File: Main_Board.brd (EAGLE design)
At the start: 160 x 100 mm, 54 parts, among them U1 RN4020RN4020, Y1 MC-30632.768K-E3, Y2 MA-5066-25.0000M-C0

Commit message: added buck regulator
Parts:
- removed S1: (no value), SparkFun-Electromechanical:SWITCH-SPDT_LOCK.007S
- removed U$11: SWITCH-SPST-2RA, SparkFun-Electromechanical:R_SW_TH
- removed U$8: LMS8117, BB8:SOT-223
- added JP1: SPDT_JUMPER, BB8:1X03
- added S2: RESET_BUTTON, BB8:5.2X5.2
- added U2: LMS8117, BB8:SOT-223
- moved FRAME4 125.5 mm to (-195.0, -178.0)
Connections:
- net 3.3V: now also JP1.3, U2.P$2, U2.P$4; no longer S1.3, U$8.P$2, U$8.P$4
- net 5V: now also U2.P$3; no longer U$8.P$3
- net GND: now also JP1.1, S2.P$3, S2.P$4, U2.P$1; no longer S1.1, U$11.P$4, U$8.P$1
- net N$23: now also JP1.2; no longer S1.2
- net N$7: now also S2.P$1, S2.P$2; no longer U$11.P$3
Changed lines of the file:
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@@
 <element name="C12" library="SparkFun-Capacitors" package="0805" value="2.2uF" x="-107" y="-95"/>
 <element name="FRAME2" library="SparkFun-Aesthetics" package="CREATIVE_COMMONS" value="FRAME-LEDGER" x="-87" y="-105"/>
-<element name="FRAME4" library="SparkFun-Aesthetics" package="CREATIVE_COMMONS" value="FRAME-LEDGER" x="-87" y="-114"/>
 <element name="FRAME1" library="SparkFun-Aesthetics" package="CREATIVE_COMMONS" value="FRAME-LEDGER" x="-87" y="-123"/>
 <element name="FRAME3" library="SparkFun-Aesthetics" package="CREATIVE_COMMONS" value="FRAME-LEDGER" x="-87" y="-132"/>
-<element name="U$8" library="BB8" package="SOT-223" value="LMS8117" x="-113" y="-132"/>
 <element name="C13" library="SparkFun-Capacitors" package="0805" value="" x="-118" y="-131"/>
 <element name="C14" library="SparkFun-Capacitors" package="0805" value="" x="-121" y="-131"/>
@@
 <element name="U$10" library="BB8" package="14-TSSOP" value="SN74LV4T125" x="-133" y="-132"/>
 <element name="C15" library="SparkFun-Capacitors" package="0805" value="4.7uF" x="-136" y="-131"/>
-<element name="U$11" library="SparkFun-Electromechanical" package="R_SW_TH" value="SWITCH-SPST-2RA" x="-152" y="-130"/>
 <element name="C16" library="SparkFun-Passives" package="0805" value=".1uF" x="-156" y="-131"/>
 <element name="C17" library="SparkFun-Passives" package="0805" value="6.8pF" x="-159" y="-137"/>
@@
 <element name="R11" library="SparkFun-Passives" package="0805" value="220" x="-171" y="-143"/>
 <element name="R12" library="SparkFun-Passives" package="0805" value="0" x="-174" y="-143"/>
-<element name="S1" library="SparkFun-Electromechanical" package="SWITCH-SPDT_LOCK.007S" value="" x="-182" y="-134"/>
 <element name="R13" library="SparkFun-Passives" package="0805" value="10K" x="-188" y="-143"/>
 <element name="R14" library="SparkFun-Passives" package="0805" value="0" x="-191" y="-143"/>
@@
 <element name="Y1" library="BB8" package="4-SMD,J-LEAD" value="MC-30632.768K-E3" x="-193" y="-150"/>
 <element name="Y2" library="BB8" package="4-SMD,J-LEAD-2" value="MA-5066-25.0000M-C0" x="-193" y="-158"/>
+<element name="S2" library="BB8" package="5.2X5.2" value="RESET_BUTTON" x="-194" y="-167"/>
+<element name="JP1" library="BB8" package="1X03" value="SPDT_JUMPER" x="-192" y="-174"/>
+<element name="FRAME4" library="SparkFun-Aesthetics" package="CREATIVE_COMMONS" value="FRAME-LEDGER" x="-195" y="-178"/>
+<element name="U2" library="BB8" package="SOT-223" value="LMS8117" x="-200" y="-178"/>
 </elements>
 <signals>
@@
 <contactref element="C11" pad="2"/>
 <contactref element="C13" pad="2"/>
-<contactref element="U$8" pad="P$1"/>
 <contactref element="C14" pad="2"/>
 <contactref element="U$9" pad="P$1"/>
@@
 <contactref element="U$10" pad="P$9"/>
 <contactref element="C15" pad="1"/>
-<contactref element="U$11" pad="P$4"/>
 <contactref element="C16" pad="1"/>
-<contactref element="S1" pad="1"/>
 <contactref element="C17" pad="1"/>
 <contactref element="C18" pad="1"/>
@@
 <contactref element="C19" pad="1"/>
 <contactref element="C16" pad="2"/>
+<contactref element="S2" pad="P$3"/>
+<contactref element="S2" pad="P$4"/>
+<contactref element="JP1" pad="1"/>
+<contactref element="U2" pad="P$1"/>
 <wire x1="-125.05" y1="-132" x2="-123.1" y2="-132" width="0" layer="19" extent="1-1"/>
 <wire x1="-127" y1="-132" x2="-125.05" y2="-132" width="0" layer="19" extent="1-1"/>
@@
 <wire x1="-120.1" y1="-131" x2="-123.1" y2="-132" width="0" layer="19" extent="1-1"/>
 <wire x1="-117.1" y1="-131" x2="-120.1" y2="-131" width="0" layer="19" extent="1-1"/>
-<wire x1="-115.3" y1="-132" x2="-117.1" y2="-131" width="0" layer="19" extent="1-1"/>
 <wire x1="-136.9" y1="-131" x2="-133" y2="-132" width="0" layer="19" extent="1-1"/>
 <wire x1="-126.35" y1="-126.4" x2="-127" y2="-132" width="0" layer="19" extent="1-1"/>
@@
 <wire x1="-129.75" y1="-126.4" x2="-126.35" y2="-126.4" width="0" layer="19" extent="1-1"/>
 <wire x1="-131.7" y1="-126.4" x2="-129.75" y2="-126.4" width="0" layer="19" extent="1-1"/>
-<wire x1="-139.9096" y1="-121.5418" x2="-131.7" y2="-126.4" width="0" layer="19" extent="1-1"/>
-<wire x1="-155.1" y1="-131" x2="-139.9096" y2="-121.5418" width="0" layer="19" extent="1-1"/>
+<wire x1="-155.1" y1="-131" x2="-136.9" y2="-131" width="0" layer="19" extent="1-1"/>
 <wire x1="-156.9" y1="-131" x2="-155.1" y2="-131" width="0" layer="19" extent="1-1"/>
 <wire x1="-159.9" y1="-137" x2="-156.9" y2="-131" width="0" layer="19" extent="1-1"/>
@@
 <wire x1="-165.9" y1="-143" x2="-162.9" y2="-137" width="0" layer="19" extent="1-1"/>
 <wire x1="-168.9" y1="-143" x2="-165.9" y2="-143" width="0" layer="19" extent="1-1"/>
-<wire x1="-182" y1="-131.2822" x2="-168.9" y2="-143" width="0" layer="19" extent="1-1"/>
+<wire x1="-188.1" y1="-163.3" x2="-168.9" y2="-143" width="0" layer="19" extent="1-1"/>
+<wire x1="-194" y1="-163.3" x2="-188.1" y2="-163.3" width="0" layer="19" extent="1-1"/>
+<wire x1="-192" y1="-174" x2="-194" y2="-163.3" width="0" layer="19" extent="1-1"/>
+<wire x1="-202.3" y1="-178" x2="-192" y2="-174" width="0" layer="19" extent="1-1"/>
 <wire x1="-106.1" y1="-95" x2="-124.4" y2="-126.4" width="0" layer="19" extent="1-1"/>
 <wire x1="-103.1" y1="-95" x2="-106.1" y2="-95" width="0" layer="19" extent="1-1"/>
@@
 <contactref element="U$3" pad="VCC"/>
 <contactref element="U$4" pad="VCC"/>
-<contactref element="U$8" pad="P$3"/>
 <contactref element="C13" pad="1"/>
 <contactref element="U$10" pad="P$14"/>
 <contactref element="U$10" pad="P$13"/>
 <contactref element="U$10" pad="P$10"/>
-<wire x1="-110.7" y1="-132" x2="-118.9" y2="-131" width="0" layer="19" extent="1-1"/>
+<contactref element="U2" pad="P$3"/>
 <wire x1="-130.4" y1="-126.4" x2="-118.9" y2="-131" width="0" layer="19" extent="1-1"/>
 <wire x1="-132.35" y1="-126.4" x2="-130.4" y2="-126.4" width="0" layer="19" extent="1-1"/>
 <wire x1="-133" y1="-126.4" x2="-132.35" y2="-126.4" width="0" layer="19" extent="1-1"/>
-<wire x1="-40.64" y1="-35.56" x2="-110.7" y2="-132" width="0" layer="19" extent="1-1"/>
+<wire x1="-197.7" y1="-178" x2="-133" y2="-126.4" width="0" layer="19" extent="1-1"/>
+<wire x1="-40.64" y1="-35.56" x2="-118.9" y2="-131" width="0" layer="19" extent="1-1"/>
 <wire x1="-15.24" y1="-13.97" x2="-40.64" y2="-35.56" width="0" layer="19" extent="1-1"/>
 </signal>
@@
 <contactref element="C10" pad="2"/>
 <contactref element="C9" pad="2"/>
-<contactref element="U$8" pad="P$2"/>
-<contactref element="U$8" pad="P$4"/>
 <contactref element="C14" pad="1"/>
 <contactref element="U$9" pad="P$14"/>
 <contactref element="U1" pad="P$23"/>
 <contactref element="C15" pad="2"/>
-<contactref element="S1" pad="3"/>
+<contactref element="JP1" pad="3"/>
+<contactref element="U2" pad="P$4"/>
+<contactref element="U2" pad="P$2"/>
 <wire x1="-121.9" y1="-131" x2="-127" y2="-126.4" width="0" layer="19" extent="1-1"/>
-<wire x1="-113" y1="-132" x2="-121.9" y2="-131" width="0" layer="19" extent="1-1"/>
-<wire x1="-113" y1="-125.7" x2="-113" y2="-132" width="0" layer="19" extent="1-1"/>
 <wire x1="-135.1" y1="-131" x2="-127" y2="-126.4" width="0" layer="19" extent="1-1"/>
-<wire x1="-100.1" y1="-95" x2="-113" y2="-125.7" width="0" layer="19" extent="1-1"/>
+<wire x1="-100.1" y1="-95" x2="-127" y2="-126.4" width="0" layer="19" extent="1-1"/>
 <wire x1="-97.1" y1="-95" x2="-100.1" y2="-95" width="0" layer="19" extent="1-1"/>
 <wire x1="-95.9" y1="-95" x2="-97.1" y2="-95" width="0" layer="19" extent="1-1"/>
@@
 <wire x1="-38.05" y1="-69.55" x2="-38.05" y2="-76.05" width="0" layer="19" extent="1-1"/>
 <wire x1="-47.55" y1="-67.55" x2="-49.55" y2="-77.05" width="0" layer="19" extent="1-1"/>
-<wire x1="-182" y1="-136.7178" x2="-135.1" y2="-131" width="0" layer="19" extent="1-1"/>
+<wire x1="-186.92" y1="-174" x2="-135.1" y2="-131" width="0" layer="19" extent="1-1"/>
+<wire x1="-200" y1="-171.7" x2="-186.92" y2="-174" width="0" layer="19" extent="1-1"/>
+<wire x1="-200" y1="-178" x2="-200" y2="-171.7" width="0" layer="19" extent="1-1"/>
 </signal>
 <signal name="N$15">
@@
 <signal name="N$7">
 <contactref element="U$5" pad="P$7"/>
-<contactref element="U$11" pad="P$3"/>
-<wire x1="-139.9096" y1="-114.506" x2="-44.55" y2="-79.05" width="0" layer="19" extent="1-1"/>
+<contactref element="S2" pad="P$1"/>
+<contactref element="S2" pad="P$2"/>
+<wire x1="-188.1" y1="-167" x2="-44.55" y2="-79.05" width="0" layer="19" extent="1-1"/>
+<wire x1="-194" y1="-167" x2="-188.1" y2="-167" width="0" layer="19" extent="1-1"/>
 </signal>
 <signal name="N$17">
@@
 <signal name="N$23">
 <contactref element="R13" pad="1"/>
-<contactref element="S1" pad="2"/>
-<wire x1="-182" y1="-134" x2="-188.9" y2="-143" width="0" layer="19" extent="1-1"/>
+<contactref element="JP1" pad="2"/>
+<wire x1="-188.9" y1="-143" x2="-189.46" y2="-174" width="0" layer="19" extent="1-1"/>
 </signal>
 <signal name="N$24">

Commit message: added jtag
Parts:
- added L1: (no value), SparkFun-Passives:0805
- added U$11: 1000uF, BB8:RADIAL_CAN_SMD
- added U$12: JTAG, BB8:IDC20
- added U$8: 100uF, BB8:RADIAL_CAN_SMD
- added U3: 5V_BUCK_REG, BB8:T0-263-6
- added Z1: SCHOTTKY_DIODE, BB8:DO-214AB2
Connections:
- new net N$31: L1.2, U3.P$2, Z1.C
- new net N$32: L1.1, U$11.P$1, U3.P$4
- net GND: now also U$11.P$2, U$8.P$2, U3.P$3, U3.P$5, U3.P$6, Z1.A
- net VCC: now also U$8.P$1, U3.P$1
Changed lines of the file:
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@@
 <element name="FRAME4" library="SparkFun-Aesthetics" package="CREATIVE_COMMONS" value="FRAME-LEDGER" x="-195" y="-178"/>
 <element name="U2" library="BB8" package="SOT-223" value="LMS8117" x="-200" y="-178"/>
+<element name="U3" library="BB8" package="T0-263-6" value="5V_BUCK_REG" x="-189" y="-189"/>
+<element name="U$8" library="BB8" package="RADIAL_CAN_SMD" value="100uF" x="-210" y="-190"/>
+<element name="Z1" library="BB8" package="DO-214AB2" value="SCHOTTKY_DIODE" x="-211" y="-195"/>
+<element name="L1" library="SparkFun-Passives" package="0805" value="" x="-215" y="-197"/>
+<element name="U$11" library="BB8" package="RADIAL_CAN_SMD" value="1000uF" x="-220" y="-198"/>
+<element name="U$12" library="BB8" package="IDC20" value="JTAG" x="-220" y="-205"/>
 </elements>
 <signals>
@@
 <contactref element="JP1" pad="1"/>
 <contactref element="U2" pad="P$1"/>
+<contactref element="U3" pad="P$5"/>
+<contactref element="U3" pad="P$3"/>
+<contactref element="U3" pad="P$6"/>
+<contactref element="U$8" pad="P$2"/>
+<contactref element="Z1" pad="A"/>
+<contactref element="U$11" pad="P$2"/>
 <wire x1="-125.05" y1="-132" x2="-123.1" y2="-132" width="0" layer="19" extent="1-1"/>
 <wire x1="-127" y1="-132" x2="-125.05" y2="-132" width="0" layer="19" extent="1-1"/>
@@
 <wire x1="-194" y1="-163.3" x2="-188.1" y2="-163.3" width="0" layer="19" extent="1-1"/>
 <wire x1="-192" y1="-174" x2="-194" y2="-163.3" width="0" layer="19" extent="1-1"/>
-<wire x1="-202.3" y1="-178" x2="-192" y2="-174" width="0" layer="19" extent="1-1"/>
+<wire x1="-189" y1="-182.2" x2="-192" y2="-174" width="0" layer="19" extent="1-1"/>
+<wire x1="-189" y1="-185.6" x2="-189" y2="-182.2" width="0" layer="19" extent="1-1"/>
+<wire x1="-199.675" y1="-185.6" x2="-189" y2="-185.6" width="0" layer="19" extent="1-1"/>
+<wire x1="-202.3" y1="-178" x2="-199.675" y2="-185.6" width="0" layer="19" extent="1-1"/>
+<wire x1="-210" y1="-185.6" x2="-199.675" y2="-185.6" width="0" layer="19" extent="1-1"/>
+<wire x1="-211" y1="-195" x2="-210" y2="-185.6" width="0" layer="19" extent="1-1"/>
+<wire x1="-220" y1="-193.6" x2="-211" y2="-195" width="0" layer="19" extent="1-1"/>
 <wire x1="-106.1" y1="-95" x2="-124.4" y2="-126.4" width="0" layer="19" extent="1-1"/>
 <wire x1="-103.1" y1="-95" x2="-106.1" y2="-95" width="0" layer="19" extent="1-1"/>
@@
 <contactref element="U$6" pad="P$1"/>
 <contactref element="U$7" pad="P$1"/>
+<contactref element="U3" pad="P$1"/>
+<contactref element="U$8" pad="P$1"/>
 <wire x1="-55" y1="-96" x2="-62" y2="-96" width="0" layer="19" extent="1-1"/>
 <wire x1="-50.43" y1="-40.64" x2="-55" y2="-96" width="0" layer="19" extent="1-1"/>
@@
 <wire x1="-1.7" y1="-1.09" x2="-1.7" y2="-1.74" width="0" layer="19" extent="1-1"/>
 <wire x1="-1.7" y1="-0.44" x2="-1.7" y2="-1.09" width="0" layer="19" extent="1-1"/>
+<wire x1="-189" y1="-189" x2="-62" y2="-96" width="0" layer="19" extent="1-1"/>
+<wire x1="-210" y1="-190" x2="-189" y2="-189" width="0" layer="19" extent="1-1"/>
 </signal>
 <signal name="N$1">
@@
 <wire x1="-158.1" y1="-137" x2="-191.9" y2="-143" width="0" layer="19" extent="1-1"/>
 </signal>
+<signal name="N$31">
+<contactref element="U3" pad="P$2"/>
+<contactref element="L1" pad="2"/>
+<contactref element="Z1" pad="C"/>
+<wire x1="-204.1" y1="-195" x2="-214.1" y2="-197" width="0" layer="19" extent="1-1"/>
+<wire x1="-189" y1="-187.3" x2="-204.1" y2="-195" width="0" layer="19" extent="1-1"/>
+</signal>
+<signal name="N$32">
+<contactref element="L1" pad="1"/>
+<contactref element="U$11" pad="P$1"/>
+<contactref element="U3" pad="P$4"/>
+<wire x1="-215.9" y1="-197" x2="-220" y2="-198" width="0" layer="19" extent="1-1"/>
+<wire x1="-189" y1="-183.9" x2="-215.9" y2="-197" width="0" layer="19" extent="1-1"/>
+</signal>
 </signals>

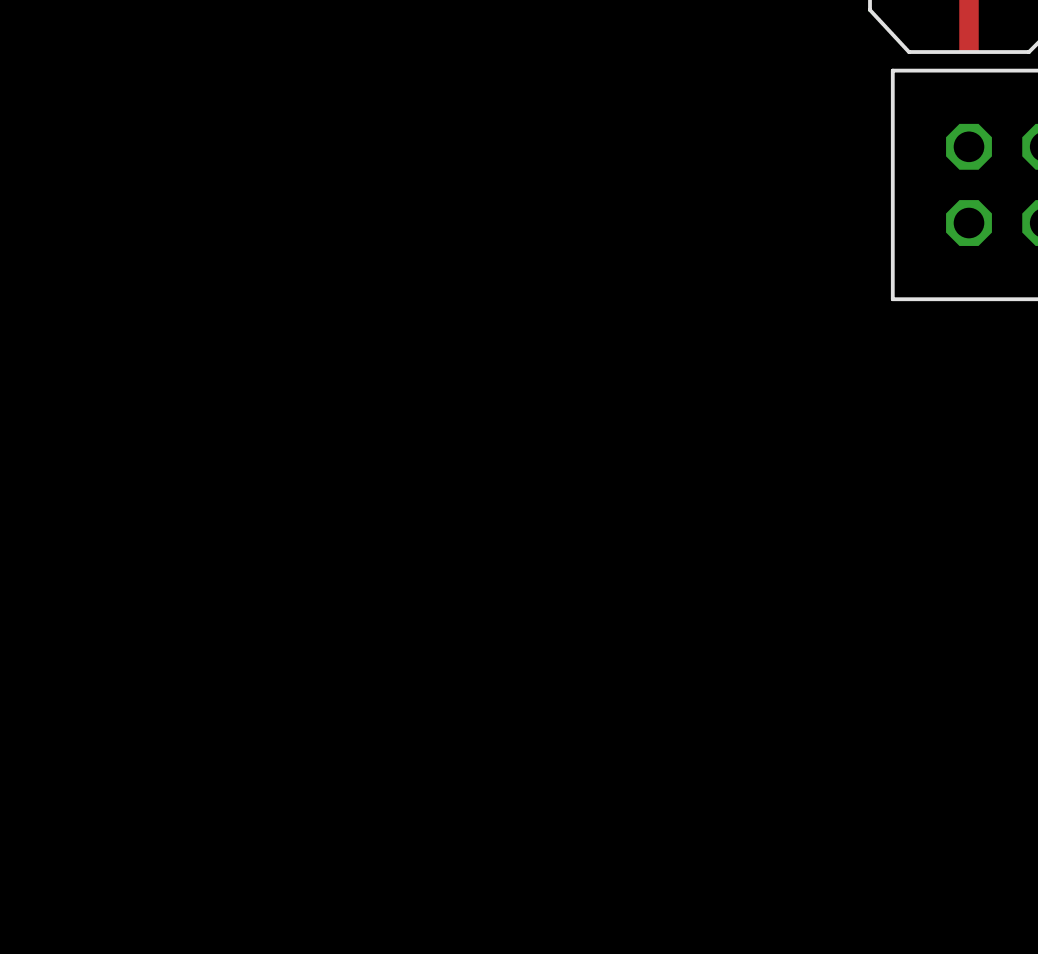
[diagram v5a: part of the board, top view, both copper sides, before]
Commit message: started adding motors
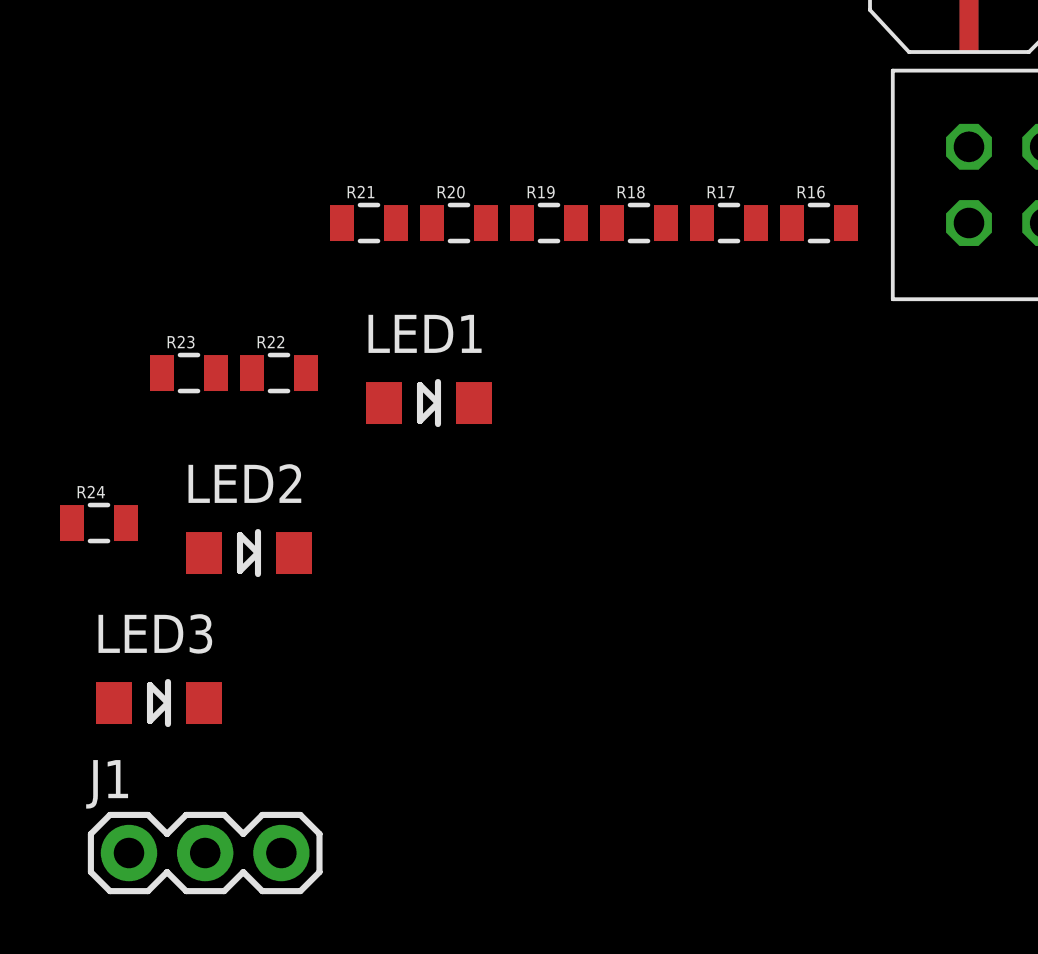
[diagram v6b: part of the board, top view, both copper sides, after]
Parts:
- added J1: (no value), SparkFun-Connectors:1X03
- added LED1, LED2, LED3: (no value), LilyPad-Wearables:LED-1206
- added R16, R17, R18, R19, R20, R21, R22, R23, R24: 10K, SparkFun-Passives:0805
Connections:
- new net !NRST: S2.P$1, S2.P$2, U$12.P$15, U$5.P$7
- new net BLUE_WAKE_SW: U$5.P$20, U1.P$7
- new net BLU_CTS: U$5.P$15, U1.P$14
- new net BLU_RTS: U$5.P$14, U1.P$18
- new net BLU_RX: U$5.P$16, U1.P$6
- new net BLU_TX: U$5.P$17, U1.P$5
- new net BLU_WAKE_HW: U$5.P$22, U1.P$15
- new net JNTRST: U$12.P$3, U$5.P$56
- new net JTCK: U$12.P$9, U$5.P$49
- new net JTDI: U$12.P$5, U$5.P$50
- new net JTDO: U$12.P$13, U$5.P$55
- new net JTMS: U$12.P$7, U$5.P$46
- new net N$33: U1.P$8
- new net N$34: R22.2, U1.P$10
- new net N$35: LED1.A, R22.1
- new net N$36: R23.2, U1.P$11
- new net N$37: R24.2, U1.P$12
- new net N$38: LED2.A, R23.1
- new net N$39: LED3.A, R24.1
- new net SERVO_PWM_3.3: U$10.P$9, U$5.P$41
- new net SERVO_PWM_5: U$10.P$8
- net 3.3V: now also U$12.P$1, U$12.P$2
- net 5V: no longer U$10.P$10
- net GND: now also LED1.C, LED2.C, LED3.C, R16.1, R17.1, R18.1, R19.1, R20.1, R21.1, U$10.P$10, U$12.P$10, U$12.P$12, U$12.P$14, U$12.P$16, U$12.P$18, U$12.P$20, U$12.P$4, U$12.P$6, U$12.P$8; no longer U$10.P$9
- net M1_A_3.3: now also U$5.P$23
- net M1_B_3.3: now also U$5.P$24
- net M2_A_3.3: now also U$5.P$25
- net M2_B_3.3: now also U$5.P$26
- net MC1_INH_3.3: now also U$5.P$40
- net MC2_IS: now also U$5.P$9
- net N$24: now also R16.2, U$12.P$11; no longer U$5.P$46
- net N$25: now also R17.2, U$12.P$17; no longer U$5.P$49
- net N$26: now also R18.2, U$12.P$19; no longer U$5.P$50
- net N$27: now also R20.2, U1.P$3; no longer U$5.P$55
- net N$28: now also R21.2, U1.P$4; no longer U$5.P$56
- net N$7: now also R19.2, U1.P$2; no longer S2.P$1, S2.P$2, U$5.P$7

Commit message: finished adding motors
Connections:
- removed net MC1_ING_3.3: U$10.P$5
- new net MC2_INH_3.3: U$5.P$39
- net MC1_IN1: now also U$5.P$38
- net MC1_IN2: now also U$5.P$37
- net MC1_INH_3.3: now also U$10.P$5
- net MC2_IN1: now also U$5.P$36
- net MC2_IN2: now also U$5.P$35
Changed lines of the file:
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@@
 <signal name="MC2_IN1">
 <contactref element="R6" pad="1"/>
+<contactref element="U$5" pad="P$36"/>
+<wire x1="-42.81" y1="-40.64" x2="-41.55" y2="-67.55" width="0" layer="19" extent="1-1"/>
 </signal>
 <signal name="MC2_IN2">
 <contactref element="R7" pad="1"/>
+<contactref element="U$5" pad="P$35"/>
+<wire x1="-39" y1="-40.64" x2="-41.05" y2="-67.55" width="0" layer="19" extent="1-1"/>
 </signal>
 <signal name="MC1_IN1">
 <contactref element="R1" pad="1"/>
+<contactref element="U$5" pad="P$38"/>
+<wire x1="-27.57" y1="-15.24" x2="-42.55" y2="-67.55" width="0" layer="19" extent="1-1"/>
 </signal>
 <signal name="MC1_IN2">
 <contactref element="R2" pad="1"/>
+<contactref element="U$5" pad="P$37"/>
+<wire x1="-31.38" y1="-15.24" x2="-42.05" y2="-67.55" width="0" layer="19" extent="1-1"/>
 </signal>
 <signal name="MC1_INH_5">
@@
 <contactref element="U$10" pad="P$2"/>
 <contactref element="U$5" pad="P$40"/>
-<wire x1="-132.35" y1="-132" x2="-43.55" y2="-67.55" width="0" layer="19" extent="1-1"/>
-</signal>
-<signal name="MC1_ING_3.3">
 <contactref element="U$10" pad="P$5"/>
+<wire x1="-130.4" y1="-132" x2="-43.55" y2="-67.55" width="0" layer="19" extent="1-1"/>
+<wire x1="-132.35" y1="-132" x2="-130.4" y2="-132" width="0" layer="19" extent="1-1"/>
 </signal>
 <signal name="N$17">
@@
 <contactref element="U$10" pad="P$8"/>
 </signal>
+<signal name="MC2_INH_3.3">
+<contactref element="U$5" pad="P$39"/>
+</signal>
 </signals>
